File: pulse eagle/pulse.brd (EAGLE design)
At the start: 18.9 x 31.1 mm, 22 parts, among them J1 ISP Touch, U1 ATMEGA328P, Y1 8MHz

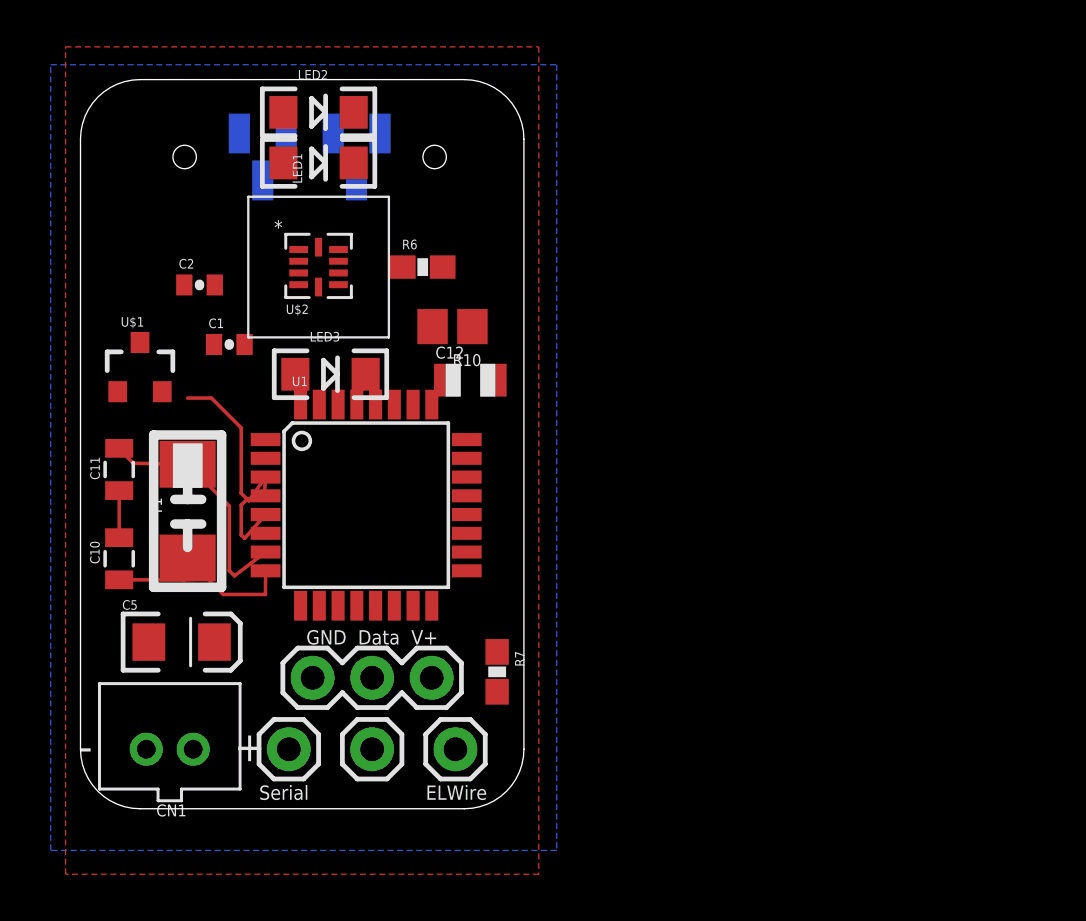
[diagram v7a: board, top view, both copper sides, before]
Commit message: Revision 4 of the board now connects all 5v, 12v, and 3.3v devices. Revision 1 of the sensor board.
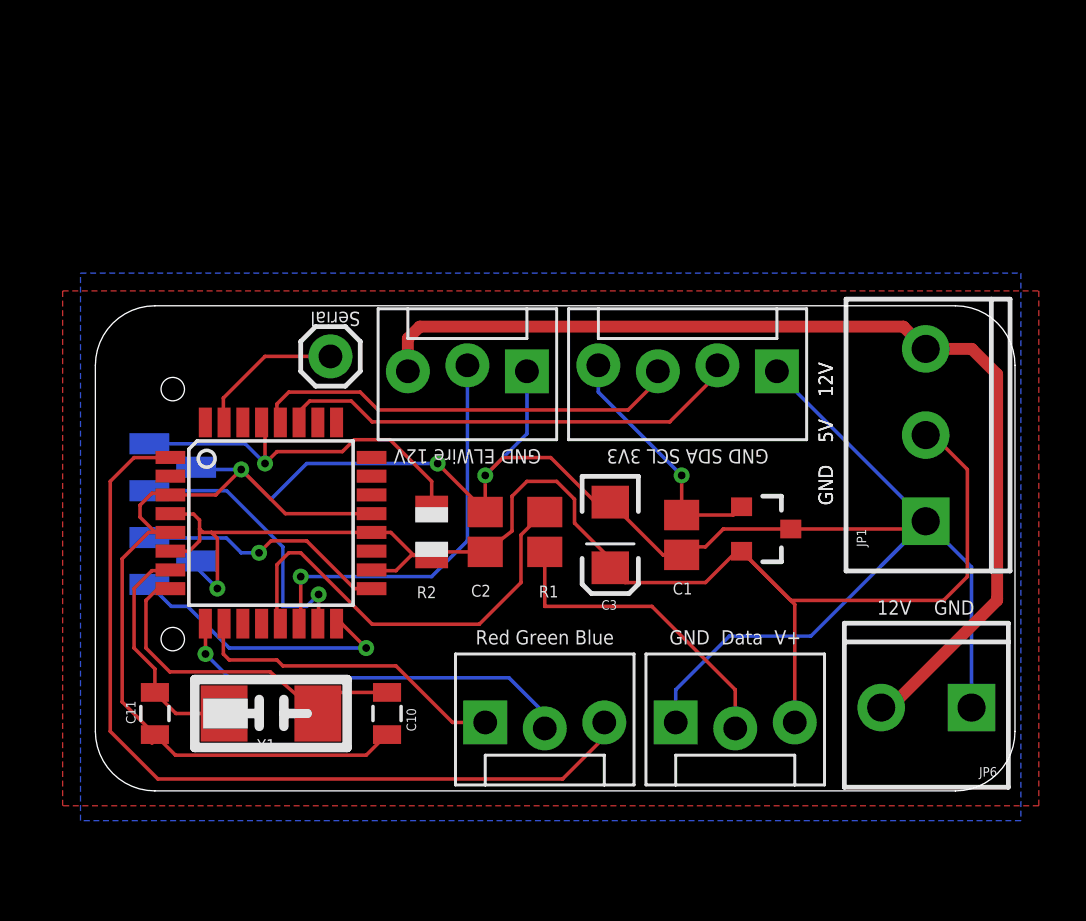
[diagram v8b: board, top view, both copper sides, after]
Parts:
- removed C12: .1uF, adafruit:C0805
- removed C5: 100uF, SparkFun-Capacitors:EIA3216
- removed CN1: (no value), adafruit:JST-PH-2-THM
- removed LED1, LED2, LED3: (no value), SparkFun-LED:LED-1206
- removed R10: 10k, adafruit:R0805
- removed R6: 1.5k, SparkFun-Resistors:0603-RES
- removed R7: 220, SparkFun-Resistors:0603-RES
- removed U$2: SI1143, pulse:SI1143
- added C3: 100uF, SparkFun-Capacitors:EIA3216
- added JP5: (no value), SparkFun-Connectors:MOLEX-1X3_LOCK
- added JP6: M023.5MM_LOCK, SparkFun-Connectors:SCREWTERMINAL-3.5MM-2_LOCK
- added R1: 220, resistor:R0805
- added R2: 10k, adafruit:R0805
- added SL2: (no value), SparkFun-Connectors:MOLEX-1X4_LOCK
- C1, C2: value 0.1uF -> .1uF; device SparkFun-Capacitors:0402-CAP -> adafruit:C0805
- JP1: value Petal -> (none); device SparkFun-Connectors:1X01 -> SparkFun-Connectors:SCREWTERMINAL-3.5MM-3_LOCK.007S
- JP3: device SparkFun-Connectors:1X01 -> SparkFun-Connectors:MOLEX-1X3_LOCK
- JP4: device SparkFun-Connectors:1X03 -> SparkFun-Connectors:MOLEX-1X3_LOCK
- Y1: value 8MHz -> 16MHz
- moved U$1 27.5 mm to (29.2, 11.9), turned to 270 degrees
- moved JP1 25.6 mm to (36.1, 12.4), turned to 90 degrees
- moved C1 20.9 mm to (25.7, 11.7), turned to 270 degrees
- moved JP2 16.9 mm to (10.7, 19.3), turned to 270 degrees
- moved JP3 16.5 mm to (19.1, 18.8), turned to 180 degrees
- moved J1 16.3 mm to (3.94, 12.6), turned to 90 degrees
- moved C2 16.1 mm to (17.3, 11.8), turned to 90 degrees
- moved JP4 15.6 mm to (25.4, 3.56)
- moved C10 13.2 mm to (13.1, 4.06), turned to 90 degrees
- moved C11 10.5 mm to (3.17, 4.06)
- moved Y1 9.34 mm to (8.13, 4.06), turned to 180 degrees
- moved U1 4.13 mm to (8.13, 12.2)
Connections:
- removed net BEATLED: JP1.1, U1.10
- removed net INT0: U$2.4, U1.32
- removed net LED1: LED1.C, U$2.9
- removed net LED2: LED2.C, U$2.6
- removed net LED3: LED3.C, U$2.7
- removed net N$2: C1.1, LED1.A, LED2.A, LED3.A, R6.2
- new net 12V: JP1.3, JP3.3, JP6.2
- new net PETALBLUE: JP5.3, U1.1
- new net PETALGREEN: JP5.2, U1.9
- new net PETALRED: JP5.1, U1.10
- net 3V3: now also C1.1, SL2.4; no longer C2.2, U$2.3
- net ELWIRE: now also JP3.2; no longer JP3.1
- net GND: now also C2.2, C3.C, JP1.1, JP3.1, JP6.1, SL2.1; no longer C12.2, C2.1, C5.C, CN1.2, U$2.8
- net N$7: now also R1.2; no longer R7.2
- net RESET: now also R2.2; no longer R10.2
- net SCL: now also SL2.3; no longer U$2.2
- net SDA: now also SL2.2; no longer U$2.1
- net STEMLED: now also R1.1; no longer R7.1
- net VCC: now also C2.1, C3.A, JP1.2, R2.1; no longer C12.1, C5.A, CN1.1, R10.1, R6.1
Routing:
- net GND: track 14.2 -> 112.5 mm, vias 0 -> 3
- net VCC: track 0.00 -> 64.8 mm, vias 0 -> 1
- net 12V: track 0.00 -> 44.1 mm
- net PETALBLUE: track 0.00 -> 37.0 mm
- net SDA: track 0.00 -> 20.1 mm
- net STEMLED: track 0.00 -> 18.7 mm
- net SCL: track 0.00 -> 18.5 mm
- net PETALGREEN: track 0.00 -> 17.5 mm, vias 0 -> 1
- net ELWIRE: track 0.00 -> 17.3 mm, vias 0 -> 1
- net RESET: track 0.00 -> 16.5 mm, vias 0 -> 1
- net PETALRED: track 0.00 -> 13.7 mm
- net N$7: track 0.00 -> 13.6 mm
- net MOSI: track 0.00 -> 12.2 mm, vias 0 -> 1
- net MISO: track 0.00 -> 12.1 mm, vias 0 -> 1
- net SCK: track 0.00 -> 10.8 mm, vias 0 -> 1
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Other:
- board size 18.9 x 31.1 mm -> 39.2 x 20.7 mm
- board text added: "12V GND"
- board text added: "GND 5V 12V"
- board text added: "GND ELWire 12V"
- board text added: "GND SDA SCL 3V3"
- board text added: "Pulse & Bloom 19 June 2014 - Rev. 4"
- board text added: "Red Green Blue"
- board text removed: "Pulse & Bloom 10 June 2014 - Rev. 3"
